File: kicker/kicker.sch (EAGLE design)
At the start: 26 parts, among them T1 NPN_BC817,215, T2 NPN_BC817,215, T3 NPN_BC817,215, T4 NPN_BC817,215, X1 JST-XH-06-PIN-LONG-PAD

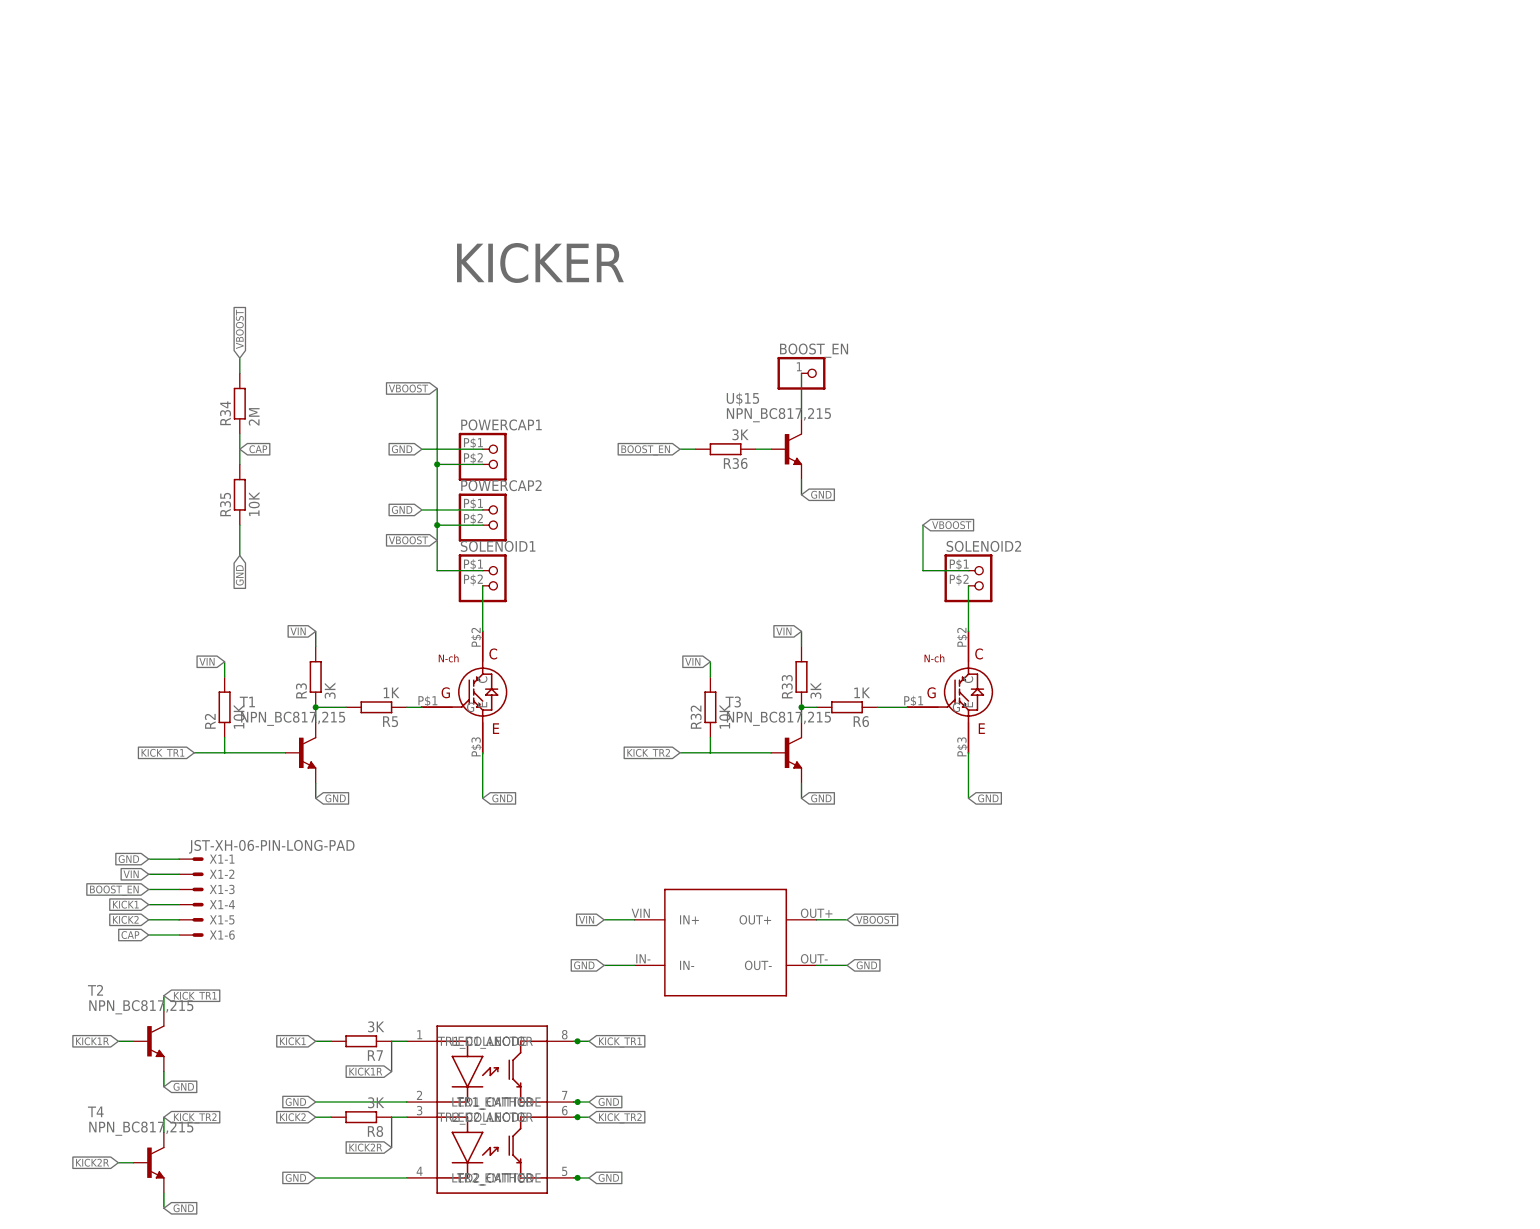
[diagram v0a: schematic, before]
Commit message: Using mos driver on kicker board
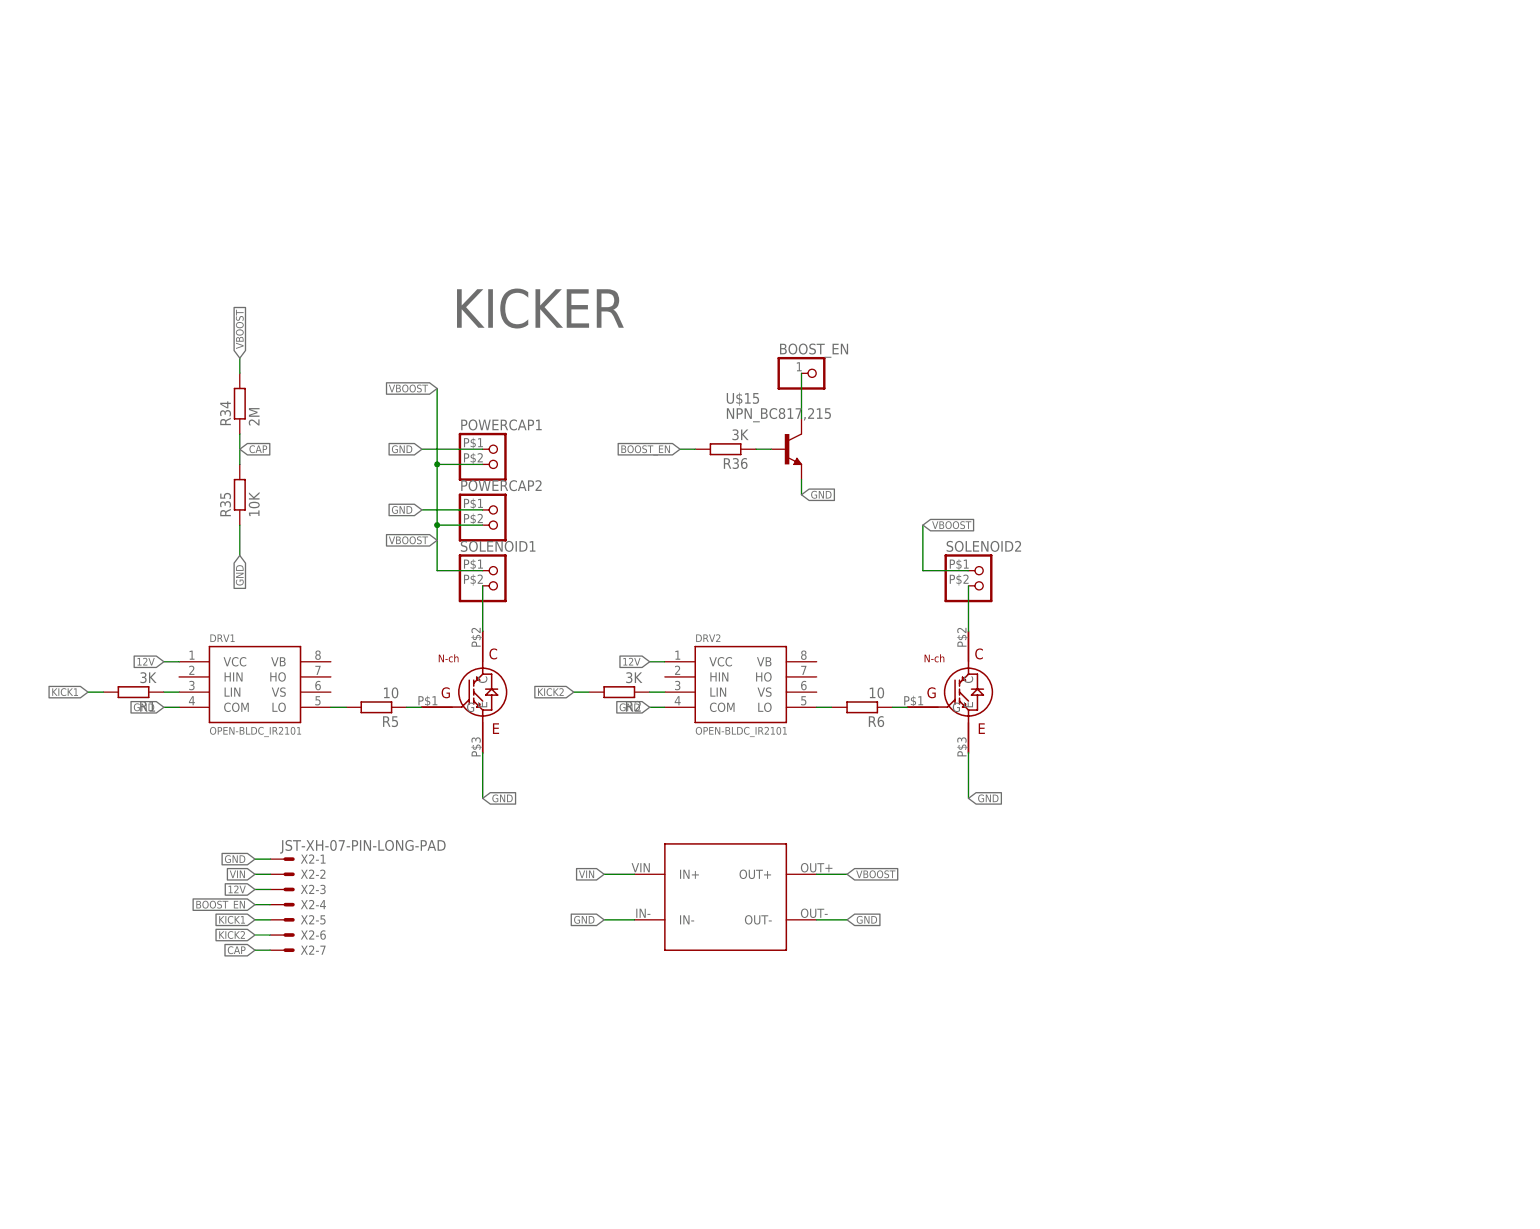
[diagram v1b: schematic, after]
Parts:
- removed R3, R33, R7, R8: 3K, rhoban:RESISTANCE-R0805
- removed R32: 10K, rhoban:RESISTANCE-R0805
- removed T1, T2, T3, T4: NPN_BC817,215, rhoban:NPN_BC817,215
- removed U$4: ACPL-227-500E, rhoban:ACPL-227-500E
- removed X1: JST-XH-06-PIN-LONG-PAD, Rembrandt Electronics - JST XH Connectors v1-0:JST-XH-06-PIN-LONG-PAD
- added DRV1, DRV2: OPEN-BLDC_IR2101, rhoban:OPEN-BLDC_IR2101
- added R1: 3K, rhoban:RESISTANCE-R0805
- added X2: JST-XH-07-PIN-LONG-PAD, Rembrandt Electronics - JST XH Connectors v1-0:JST-XH-07-PIN-LONG-PAD
- R2: value 10K -> 3K
- R5, R6: value 1K -> 10
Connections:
- removed net KICK1R: R7.1, T2.B, U$4.LED1_ANODE
- removed net KICK2R: R8.1, T4.B, U$4.LED2_ANODE
- removed net KICK_TR1: R2.1, T1.B, T2.C, U$4.TR1_COLLECTOR
- removed net KICK_TR2: R32.1, T3.B, T4.C, U$4.TR2_COLLECTOR
- removed net N$35: R33.1, R6.2, T3.C
- removed net N$4: R3.1, R5.2, T1.C
- new net 12V: DRV1.VCC, DRV2.VCC, X2-3.S
- new net N$1: DRV2.LIN, R2.1
- new net N$3: DRV2.LO, R6.2
- new net N$5: DRV1.LIN, R1.1
- new net N$9: DRV1.LO, R5.2
- net BOOST_EN: now also X2-4.S; no longer X1-3.S
- net CAP: now also X2-7.S; no longer X1-6.S
- net GND: now also DRV1.COM, DRV2.COM, X2-1.S; no longer T1.E, T2.E, T3.E, T4.E, U$4.LED1_CATHODE, U$4.LED2_CATHODE, U$4.TR1_EMITTER, U$4.TR2_EMITTER, X1-1.S
- net KICK1: now also R1.2, X2-5.S; no longer R7.2, X1-4.S
- net KICK2: now also R2.2, X2-6.S; no longer R8.2, X1-5.S
- net VIN: now also X2-2.S; no longer R2.2, R3.2, R32.2, R33.2, X1-2.S
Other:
- moved on the sheet: R2, R6

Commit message: kicker board routed
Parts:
- added C1, C2: (no value), rcl:C-EUC0805
- added D1, D5: (no value), diode:ZENER-DIODESOD80C
- added D2, D3: 1N6267A, diode:1N6267A
- added D4: RED, SparkFun:LED1206
- added Q1, Q2: BSS123, transistor-small-signal:BSS123
- added R10, R11, R9: 10K, rhoban:RESISTANCE-R0805
- added R3: 1M, rhoban:RESISTANCE-R0805
- added R4, R7, R8: 3K, rhoban:RESISTANCE-R0805
- R34: value 2M -> 1M
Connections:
- new net N$10: Q2.S, R9.2
- new net N$11: D4.A, R9.1
- new net N$12: Q1.S, Q2.D
- new net N$13: DRV1.HIN, R7.1
- new net N$14: Q1.G, R10.1, R11.2
- new net N$16: D5.C, Q2.G, R11.1
- new net N$4: R3.1, R34.2
- new net N$6: DRV2.HIN, R4.1
- net 12V: now also C1.1, C2.1, DRV1.VB, DRV2.VB
- net CAP: now also D1.C
- net GND: now also C1.2, C2.2, D1.A, D4.C, D5.A, DRV1.VS, DRV2.VS, R4.2, R7.2, R8.2
- net N$2: now also D2.A
- net N$36: now also D3.A
- net N$38: now also R8.1
- net VBOOST: now also D2.C, D3.C, Q1.D, R10.2, R3.2; no longer R34.2
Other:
- note added: "RED"
- moved on the sheet: BOOST_EN, DRV1, DRV2, POWERCAP1, POWERCAP2, R1, R2, R34, R35, R36, R5, R6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

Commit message: Values
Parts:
- C1, C2: value (none) -> 1uF
- D1: value (none) -> 3.9V; FARNELL (none) -> 1097198
- D2, D3: FARNELL (none) -> 9551735
- D5: value (none) -> 12V; FARNELL (none) -> 2319144
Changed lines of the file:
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@@
 <part name="GND15" library="supply1" deviceset="GND" device=""/>
 <part name="GND16" library="supply1" deviceset="GND" device=""/>
-<part name="D2" library="diode" deviceset="1N6267A" device=""/>
-<part name="D3" library="diode" deviceset="1N6267A" device=""/>
-<part name="C1" library="rcl" deviceset="C-EU" device="C0805"/>
-<part name="C2" library="rcl" deviceset="C-EU" device="C0805"/>
+<part name="D2" library="diode" deviceset="1N6267A" device="">
+<attribute name="FARNELL" value="9551735"/>
+</part>
+<part name="D3" library="diode" deviceset="1N6267A" device="">
+<attribute name="FARNELL" value="9551735"/>
+</part>
+<part name="C1" library="rcl" deviceset="C-EU" device="C0805" value="1uF"/>
+<part name="C2" library="rcl" deviceset="C-EU" device="C0805" value="1uF"/>
 <part name="GND17" library="supply1" deviceset="GND" device=""/>
 <part name="GND18" library="supply1" deviceset="GND" device=""/>
@@
 </part>
 <part name="GND21" library="supply1" deviceset="GND" device=""/>
-<part name="D5" library="diode" deviceset="ZENER-DIODE" device="SOD80C"/>
-<part name="D1" library="diode" deviceset="ZENER-DIODE" device="SOD80C"/>
+<part name="D5" library="diode" deviceset="ZENER-DIODE" device="SOD80C" value="12V">
+<attribute name="FARNELL" value="2319144"/>
+</part>
+<part name="D1" library="diode" deviceset="ZENER-DIODE" device="SOD80C" value="3.9V">
+<attribute name="FARNELL" value="1097198"/>
+</part>
 </parts>
 <sheets>
@@
 <instance part="GND15" gate="1" x="-20.32" y="0"/>
 <instance part="GND16" gate="1" x="78.74" y="0"/>
-<instance part="D2" gate="1" x="137.16" y="48.26" rot="R90"/>
-<instance part="D3" gate="1" x="33.02" y="48.26" rot="R90"/>
+<instance part="D2" gate="1" x="137.16" y="48.26" rot="R90">
+<attribute name="FARNELL" x="137.16" y="48.26" size="1.778" layer="96" rot="R90" display="off"/>
+</instance>
+<instance part="D3" gate="1" x="33.02" y="48.26" rot="R90">
+<attribute name="FARNELL" x="33.02" y="48.26" size="1.778" layer="96" rot="R90" display="off"/>
+</instance>
 <instance part="C1" gate="G$1" x="-22.86" y="35.56"/>
 <instance part="C2" gate="G$1" x="76.2" y="35.56"/>
@@
 </instance>
 <instance part="GND21" gate="1" x="58.42" y="66.04"/>
-<instance part="D5" gate="G$1" x="58.42" y="76.2" rot="R90"/>
-<instance part="D1" gate="G$1" x="119.38" y="96.52" rot="R90"/>
+<instance part="D5" gate="G$1" x="58.42" y="76.2" rot="R90">
+<attribute name="FARNELL" x="58.42" y="76.2" size="1.778" layer="96" rot="R90" display="off"/>
+</instance>
+<instance part="D1" gate="G$1" x="119.38" y="96.52" rot="R90">
+<attribute name="FARNELL" x="119.38" y="96.52" size="1.778" layer="96" rot="R90" display="off"/>
+</instance>
 </instances>
 <busses>

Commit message: Passive values
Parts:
- R1, R2, R4, R7: value 3K -> 470
- R10, R11: value 10K -> 100K
- R8: value 3K -> 100K
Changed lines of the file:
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@@
 <attribute name="FARNELL" value="8638730"/>
 </part>
-<part name="R1" library="rhoban" deviceset="RESISTANCE" device="-R0805" value="3K">
+<part name="R1" library="rhoban" deviceset="RESISTANCE" device="-R0805" value="470">
 <attribute name="FARNELL" value="2446965"/>
 </part>
@@
 <attribute name="FARNELL" value="8638730"/>
 </part>
-<part name="R2" library="rhoban" deviceset="RESISTANCE" device="-R0805" value="3K">
+<part name="R2" library="rhoban" deviceset="RESISTANCE" device="-R0805" value="470">
 <attribute name="FARNELL" value="2446965"/>
 </part>
@@
 <part name="GND11" library="supply1" deviceset="GND" device=""/>
 <part name="GND12" library="supply1" deviceset="GND" device=""/>
-<part name="R4" library="rhoban" deviceset="RESISTANCE" device="-R0805" value="3K">
+<part name="R4" library="rhoban" deviceset="RESISTANCE" device="-R0805" value="470">
 <attribute name="FARNELL" value="2446965"/>
 </part>
-<part name="R7" library="rhoban" deviceset="RESISTANCE" device="-R0805" value="3K">
+<part name="R7" library="rhoban" deviceset="RESISTANCE" device="-R0805" value="470">
 <attribute name="FARNELL" value="2446965"/>
 </part>
@@
 <part name="GND17" library="supply1" deviceset="GND" device=""/>
 <part name="GND18" library="supply1" deviceset="GND" device=""/>
-<part name="R8" library="rhoban" deviceset="RESISTANCE" device="-R0805" value="3K">
+<part name="R8" library="rhoban" deviceset="RESISTANCE" device="-R0805" value="100K">
 <attribute name="FARNELL" value="2446965"/>
 </part>
@@
 <attribute name="FARNELL" value="2447553"/>
 </part>
-<part name="R10" library="rhoban" deviceset="RESISTANCE" device="-R0805" value="10K">
+<part name="R10" library="rhoban" deviceset="RESISTANCE" device="-R0805" value="100K">
 <attribute name="FARNELL" value="2447553"/>
 </part>
-<part name="R11" library="rhoban" deviceset="RESISTANCE" device="-R0805" value="10K">
+<part name="R11" library="rhoban" deviceset="RESISTANCE" device="-R0805" value="100K">
 <attribute name="FARNELL" value="2447553"/>
 </part>
